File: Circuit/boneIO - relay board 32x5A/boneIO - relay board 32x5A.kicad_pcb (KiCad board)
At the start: 2 copper layers, 197 x 102 mm, 81 parts, among them J1 Screw_Terminal_01x03, J10 Screw_Terminal_01x03, J11 Screw_Terminal_01x03, J12 Conn_02x04_Odd_Even, J13 Screw_Terminal_01x03, J14 Screw_Terminal_01x03, J15 Screw_Terminal_01x03, J16 Screw_Terminal_01x03, J17 Screw_Terminal_01x03, J2 Screw_Terminal_01x03, J3 Screw_Terminal_01x03, J4 Screw_Terminal_01x03, J5 Screw_Terminal_01x03, J6 Screw_Terminal_01x03, J7 Screw_Terminal_01x03, J8 Screw_Terminal_01x03, J9 Screw_Terminal_01x03, K1 HF46F, K10 HF46F, K11 HF46F, K12 HF46F, K13 HF46F, K14 HF46F, K15 HF46F, K16 HF46F, K17 HF46F, K18 HF46F, K19 HF46F, K2 HF46F, K20 HF46F, K21 HF46F, K22 HF46F, K23 HF46F, K24 HF46F, K25 HF46F, K26 HF46F, K27 HF46F, K28 HF46F, K29 HF46F, K3 HF46F, K30 HF46F, K31 HF46F, K32 HF46F, K4 HF46F, K5 HF46F, K6 HF46F, K7 HF46F, K8 HF46F, K9 HF46F, SW1 SW_DIP_x03, SW2 SW_DIP_x03, SW3 SW_DIP_x03, U1 MCP23017_SS, U2 ULN2803A, U3 ULN2803A, U4 MCP23017_SS, U5 ULN2803A, U6 ULN2803A, U7 MCP9808_MSOP

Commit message: 32x5 v0.3
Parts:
- removed the R2 at (348.6, 320.5)
- removed the R6 at (426.2, 320.7)
- removed SW1, SW2, SW3: SW_DIP_x03, Button_Switch_SMD:SW_DIP_SPSTx03_Slide_KingTek_DSHP03TJ_W5.25mm_P1.27mm_JPin
- added C7: 100n, Capacitor_SMD:C_0603_1608Metric, F.Cu at (476.8, 314.4)
- added JP1: NO_Small, Jumper:SolderJumper-2_P1.3mm_Open_RoundedPad1.0x1.5mm, F.Cu at (340.0, 322.9)
- added JP10: NO_Small, Jumper:SolderJumper-2_P1.3mm_Open_RoundedPad1.0x1.5mm, F.Cu at (473.0, 309.5)
- added JP2: NO_Small, Jumper:SolderJumper-2_P1.3mm_Open_RoundedPad1.0x1.5mm, F.Cu at (340.0, 320.8)
- added JP3: NO_Small, Jumper:SolderJumper-2_P1.3mm_Open_RoundedPad1.0x1.5mm, F.Cu at (340.0, 318.7)
- added JP4: NO_Small, Jumper:SolderJumper-2_P1.3mm_Open_RoundedPad1.0x1.5mm, F.Cu at (417.3, 318.2)
- added JP5: NO_Small, Jumper:SolderJumper-2_P1.3mm_Open_RoundedPad1.0x1.5mm, F.Cu at (417.3, 320.4)
- added JP6: NO_Small, Jumper:SolderJumper-2_P1.3mm_Open_RoundedPad1.0x1.5mm, F.Cu at (417.3, 322.5)
- added JP8: NO_Small, Jumper:SolderJumper-2_P1.3mm_Open_RoundedPad1.0x1.5mm, F.Cu at (473.0, 305.2)
- added JP9: NO_Small, Jumper:SolderJumper-2_P1.3mm_Open_RoundedPad1.0x1.5mm, F.Cu at (473.0, 307.3)
- added R15: 4.7k, Resistor_SMD:R_0603_1608Metric, F.Cu at (475.0, 314.4)
- added R4: 10k, Resistor_SMD:R_0603_1608Metric, F.Cu at (344.7, 318.8)
- added R8: 10k, Resistor_SMD:R_0603_1608Metric, F.Cu at (422.0, 322.1)
- added U8: MCP9808_MSOP, Package_SO:MSOP-8_3x3mm_P0.65mm, F.Cu at (468.9, 314.5)
- J12: footprint ph80ds-21:PinHeader_2x04_P2.54mm_Vertical -> Connector_PinHeader_2.54mm:PinHeader_2x04_P2.54mm_Vertical
- K1, K10, K11, K12, K13, K14, K15, K16, K17, K18, K19, K2, K20, K21, K22, K23, K24, K25, K26, K27, K28, K29, K3, K30, K31, K32, K4, K5, K6, K7, K8, K9: footprint HF46F:HF46F -> boneIO_LOGO:HF46F
- U7: value MCP9808_MSOP -> MCP9808_SO8; footprint Package_SO:MSOP-8_3x3mm_P0.65mm -> Package_SO:SO-8_3.9x4.9mm_P1.27mm
- moved R11 11.3 mm to (466.7, 305.7)
- moved R12 7.86 mm to (466.7, 307.4)
- moved R14 6.99 mm to (475.8, 311.7), turned to 0 degrees
- moved R5 5.67 mm to (422.0, 318.5)
- moved R13 4.57 mm to (466.7, 309.1)
- moved R7 4.34 mm to (422.0, 320.3)
- moved U7 4.27 mm to (468.9, 314.3), turned to 0 degrees
- moved R3 4.20 mm to (344.7, 320.6)
- moved R1 3.89 mm to (344.7, 322.4)
- renumbered JP1 to JP7, R4 to R2, R8 to R6
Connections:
- R1 pad 1: Net-(R1-Pad1) -> Net-(JP1-Pad2)
- R11 pad 1: Net-(R11-Pad1) -> Net-(JP8-Pad2)
- R13 pad 1: Net-(R13-Pad1) -> Net-(JP10-Pad2)
- R3 pad 1: Net-(R3-Pad1) -> Net-(JP2-Pad2)
- R5 pad 1: Net-(R5-Pad1) -> Net-(JP4-Pad2)
- R7 pad 1: Net-(R7-Pad1) -> Net-(JP5-Pad2)
- U1 pad 15: Net-(R1-Pad1) -> Net-(JP3-Pad2)
- U1 pad 16: Net-(R2-Pad1) (its old number) -> Net-(JP2-Pad2)
- U1 pad 17: Net-(R3-Pad1) -> Net-(JP1-Pad2)
- U4 pad 15: Net-(R5-Pad1) -> Net-(JP6-Pad2)
- U4 pad 16: Net-(R6-Pad1) (its old number) -> Net-(JP5-Pad2)
- U4 pad 17: Net-(R7-Pad1) -> Net-(JP4-Pad2)
- U7 pad 5: Net-(R11-Pad1) -> Net-(JP10-Pad2)
- U7 pad 7: Net-(R13-Pad1) -> Net-(JP8-Pad2)
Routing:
- net Net-(JP10-Pad2): track 0.00 -> 20.0 mm, vias 0 -> 3
- net Net-(R15-Pad2): track 0.00 -> 19.5 mm, vias 0 -> 2
- net Net-(JP8-Pad2): track 0.00 -> 19.3 mm, vias 0 -> 2
- net Net-(R14-Pad2): track 3.66 -> 21.5 mm, vias 0 -> 2
- net Net-(JP1-Pad2): track 0.00 -> 17.3 mm, vias 0 -> 2
- net Net-(JP6-Pad2): track 0.00 -> 15.9 mm, vias 0 -> 2
- net Net-(R6-Pad1) (its old number): track 15.1 -> 0.00 mm
- net Net-(R2-Pad1) (its old number): track 15.1 -> 0.00 mm
- net Net-(R13-Pad1): track 14.2 -> 0.00 mm
- net Net-(JP2-Pad2): track 0.00 -> 13.5 mm
- net Net-(R5-Pad1): track 12.8 -> 0.00 mm
- net Net-(R1-Pad1): track 12.5 -> 0.00 mm
- net Net-(R3-Pad1): track 12.0 -> 0.00 mm
- net Net-(R11-Pad1): track 12.0 -> 0.00 mm
- net Net-(R7-Pad1): track 11.2 -> 0.00 mm
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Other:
- board text added: "Relay Board 32x5A v0.3"
- board text removed: "Relay Board 32x5A v0.1"

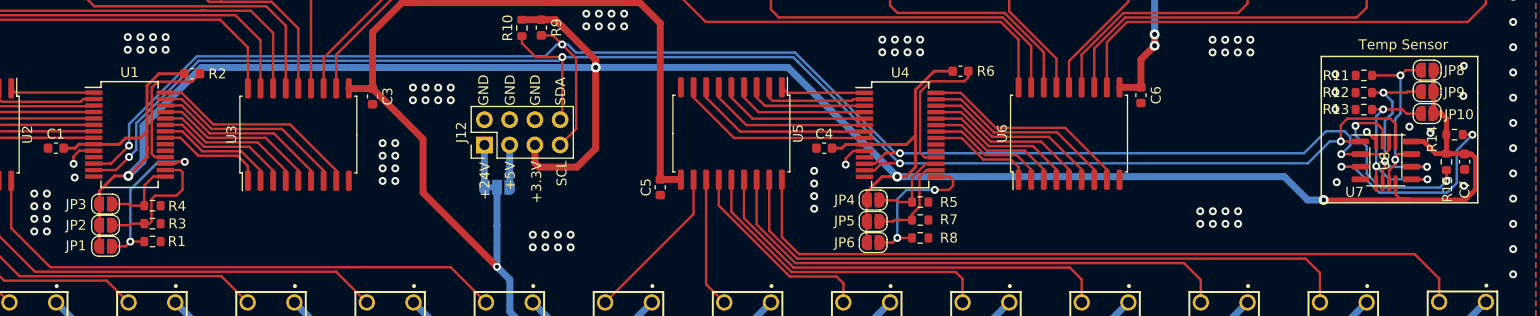
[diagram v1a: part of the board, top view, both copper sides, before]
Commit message: Update boneIO - relay board 32x5A.kicad_pcb
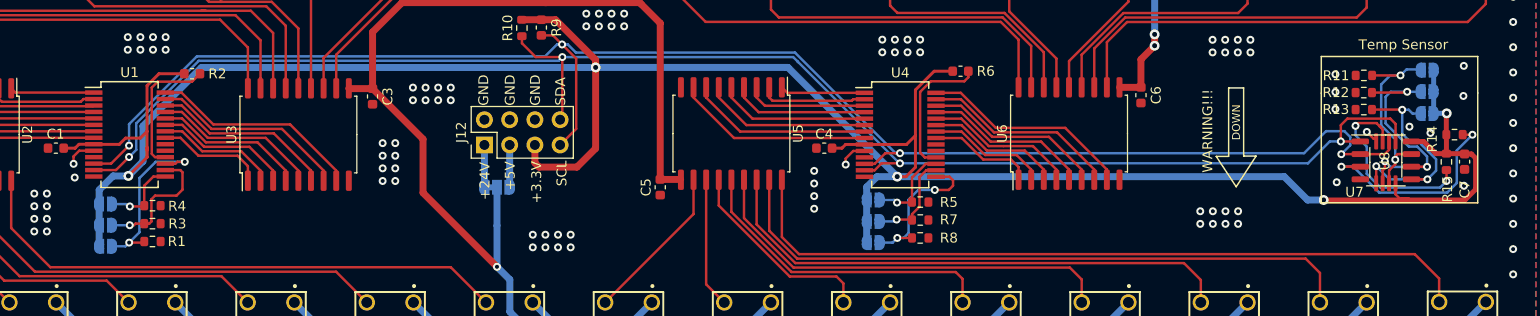
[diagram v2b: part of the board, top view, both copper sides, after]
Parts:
- A0: renamed from JP8; moved to B.Cu
- A0: renamed from JP6; moved to B.Cu
- A0: renamed from JP3; moved to B.Cu
- A1: renamed from JP9; moved to B.Cu
- A1: renamed from JP5; moved to B.Cu
- A1: renamed from JP2; moved to B.Cu
- A2: renamed from JP10; moved to B.Cu
- A2: renamed from JP4; moved to B.Cu
- A2: renamed from JP1; moved to B.Cu
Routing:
- net Net-(JP9-Pad2): track 21.4 -> 25.1 mm
- net Net-(JP10-Pad2): track 20.0 -> 23.3 mm
- net Net-(JP8-Pad2): track 19.3 -> 21.2 mm
- net +3V3: track 263.5 -> 264.4 mm, vias 4 -> 5
- net Net-(JP5-Pad2): track 10.1 -> 9.93 mm, vias 0 -> 1
- net Net-(JP3-Pad2): track 7.83 -> 7.89 mm, vias 0 -> 1
- net Net-(JP4-Pad2): track 8.79 -> 8.83 mm, vias 0 -> 1
- net Net-(JP2-Pad2): vias 0 -> 1
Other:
- board text added: "DOWN"
- board text added: "WARNING!!!"
